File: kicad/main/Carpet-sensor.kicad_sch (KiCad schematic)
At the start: 11 parts, among them Q18 AO3400

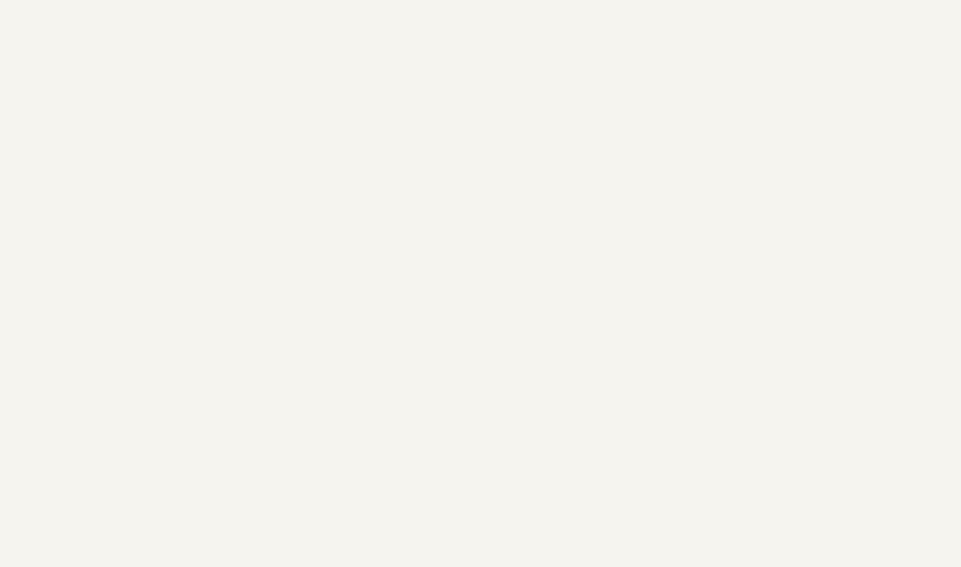
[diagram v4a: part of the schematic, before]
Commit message: Cleaned up schematic filenames
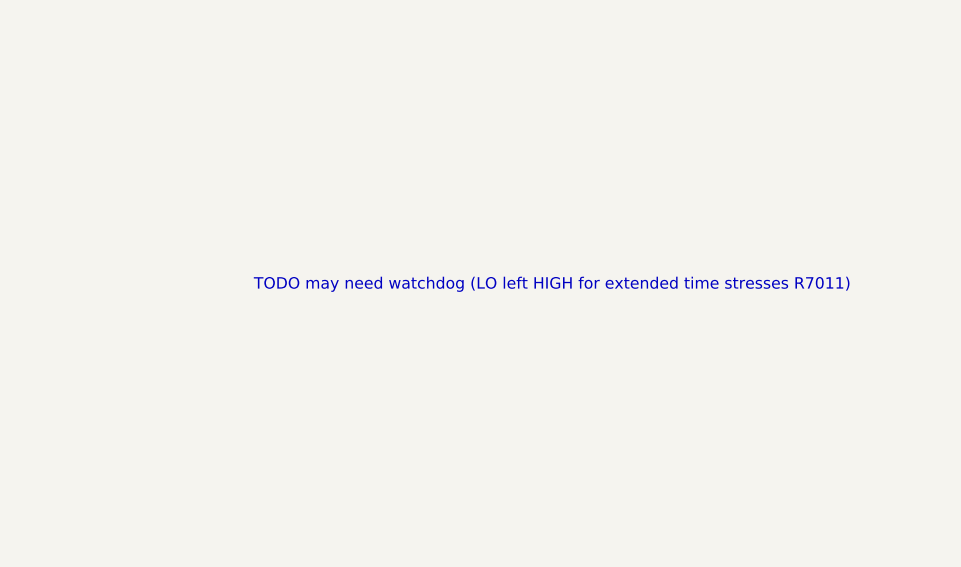
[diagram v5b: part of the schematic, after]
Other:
- note added: "TODO may need watchdog (LO left HIGH for extended time stresses R7011)"
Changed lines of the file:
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@@
+		)
+	)
+	(text "TODO may need watchdog (LO left HIGH for extended time stresses R7011)"
+		(exclude_from_sim no)
+		(at 387.35 156.972 0)
+		(effects
+			(font
+				(size 1.27 1.27)
+				(color 255 0 255 1)
+			)
 		)
 	)
